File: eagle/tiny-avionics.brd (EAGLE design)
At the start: 65.8 x 25.4 mm, 60 parts, among them J1 USB-MICROB, J3 JST-PH-2-SMT-RA, U1 LP5907, U5 LTC1998, U6 ATMEGA32U4-AU, X1 8MHz

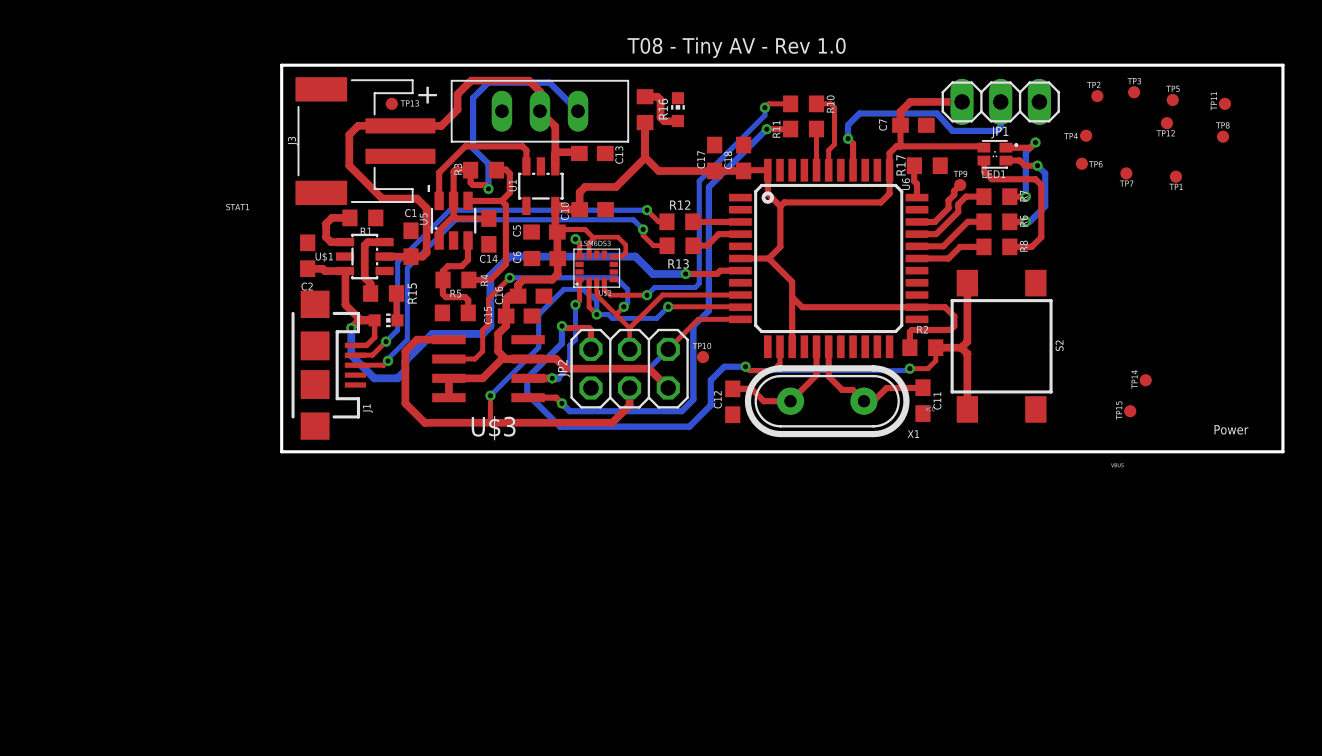
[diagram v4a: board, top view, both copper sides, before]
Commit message: Finished new board layout with no DRC errors.
It's a little smaller, but not much smaller.  Made an effort to spread out
components for easier assembly, however.  Layout is also much more
intuitive.
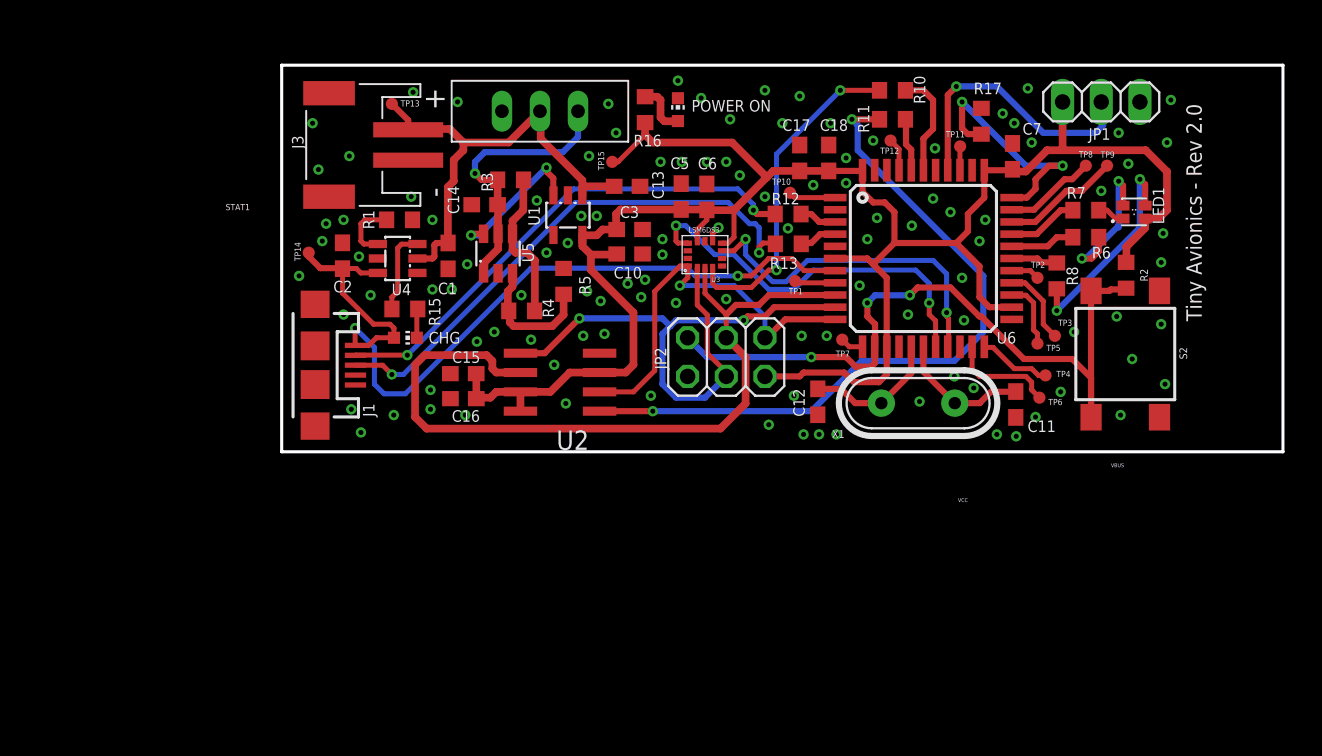
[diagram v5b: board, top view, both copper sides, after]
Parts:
- removed U$1: BQ21040, tinyav-lib:SOT23-6L
- removed U$2: LSM6DS3, tinyav-lib:LGA-14L
- removed U$3: M25PX16, tinyav-lib:SO8
- added C3: 2.2µ, rcl:C0603
- added U2: M25PX16, tinyav-lib:SO8
- added U3: LSM6DS3, tinyav-lib:LGA-14L
- added U4: BQ21040, tinyav-lib:SOT23-6L
- moved TP14 55.6 mm to (1.78, 13.1)
- moved TP15 37.8 mm to (21.7, 19.1)
- moved TP1 25.9 mm to (33.7, 11.2)
- moved TP7 21.6 mm to (36.8, 7.37)
- moved TP5 18.3 mm to (49.7, 7.11)
- moved TP12 18.2 mm to (40.0, 20.4)
- moved TP11 17.6 mm to (44.6, 20.1)
- moved TP3 16.8 mm to (50.8, 7.62)
- moved TP4 16.0 mm to (50.2, 5.02)
- moved TP6 15.6 mm to (49.8, 3.56)
- moved R2 14.2 mm to (55.5, 11.6), turned to 90 degrees
- moved TP2 12.6 mm to (49.7, 11.4)
- moved TP10 12.2 mm to (33.4, 17.0)
- moved C6 11.4 mm to (27.9, 16.7), turned to 90 degrees
- moved LED1 9.91 mm to (56.0, 15.7), turned to 90 degrees
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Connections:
- net CLK: now also U2.6, U3.13; no longer U$2.13, U$3.6
- net GND: now also C3.2, U2.4, U3.2, U3.3, U3.6, U3.7, U4.5; no longer U$1.5, U$2.2, U$2.3, U$2.6, U$2.7, U$3.4
- net MEM_EN: now also U2.1; no longer U$3.1
- net MISO: now also U2.2, U3.1; no longer U$2.1, U$3.2
- net MOSI: now also U2.5, U3.14; no longer U$2.14, U$3.5
- net N$10: now also U3.4; no longer U$2.4
- net N$11: now also U3.9; no longer U$2.9
- net N$13: now also U4.2; no longer U$1.2
- net N$4: now also U4.3; no longer U$1.3
- net N$49: now also U4.4; no longer U$1.4
- net VBUS1: now also U4.6; no longer U$1.6
- net VCC: now also C3.1, U2.3, U2.7, U2.8, U3.5, U3.8; no longer U$2.5, U$2.8, U$3.3, U$3.7, U$3.8
- net XM_EN: now also U3.12; no longer U$2.12
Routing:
- net N$10: track 1.27 -> 25.4 mm, vias 1 -> 2
- net N$11: track 0.00 -> 22.6 mm, vias 0 -> 2
- net CLK: track 31.6 -> 51.8 mm, vias 2 -> 0
- net VCC: track 114.5 -> 131.7 mm
- net N$65: track 2.18 -> 16.1 mm, vias 0 -> 2
- net MEM_EN: track 32.9 -> 46.7 mm
- net MOSI: track 49.9 -> 39.4 mm, vias 3 -> 2
- net VBUS1: track 45.6 -> 54.9 mm
- net D+: track 28.2 -> 35.4 mm
- net N$15: track 25.1 -> 18.1 mm
- net TP6: track 0.00 -> 6.96 mm
- net N$13: track 36.9 -> 30.7 mm
- net TP8: track 0.00 -> 6.07 mm
- net N$3: track 54.2 -> 48.2 mm
- net D-: track 27.3 -> 33.0 mm
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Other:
- board text added: "CHG"
- board text added: "POWER ON"
- board text added: "Tiny Avionics - Rev 2.0"
- board text removed: "Power"
- board text removed: "T08 - Tiny AV - Rev 1.0"

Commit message: Some minor changes.
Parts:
- moved R2 0.13 mm to (55.5, 11.5)
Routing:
- net GND: vias 111 -> 112
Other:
- board text removed: "STAT1"
- board text removed: "VBUS"
- board text removed: "VCC"
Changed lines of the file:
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@@
 <text x="59.436" y="22.86" size="1.016" layer="21" font="vector" rot="R270">Tiny Avionics - Rev 2.0</text>
 <text x="26.924" y="22.352" size="0.762" layer="21">POWER ON</text>
-<text x="-3.683" y="15.875" size="0.4064" layer="21">STAT1</text>
-<text x="54.483" y="-1.016" size="0.254" layer="21" font="vector">VBUS</text>
-<text x="45.085" y="-3.048" size="0.254" layer="21" font="vector" rot="R180">VCC</text>
 <text x="23.495" y="27.94" size="1.778" layer="150">Tiny AV Board Layout
 Rev: 1.0
@@
 <attribute name="NAME" x="36.987" y="1.418" size="0.508" layer="25" ratio="10" rot="R180"/>
 </element>
-<element name="R2" library="rcl" package="R0603" value="10k" x="55.481" y="11.597" smashed="yes" rot="R90">
-<attribute name="NAME" x="56.406" y="12.025" size="0.508" layer="25" ratio="10" rot="R270"/>
+<element name="R2" library="rcl" package="R0603" value="10k" x="55.481" y="11.47" smashed="yes" rot="R90">
+<attribute name="NAME" x="56.406" y="11.898" size="0.508" layer="25" ratio="10" rot="R270"/>
 </element>
 <element name="JP1" library="pinhead" package="1X03" value="" x="53.848" y="22.987" smashed="yes">
@@
 <via x="8.636" y="23.622" extent="1-16" drill="0.3302"/>
 <via x="4.064" y="9.017" extent="1-16" drill="0.3302"/>
+<via x="48.514" y="7.62" extent="1-16" drill="0.3302"/>
 <wire x1="26.683" y1="13.204" x2="27.813" y2="13.834" width="0" layer="19" extent="1-1"/>
-<wire x1="47.964" y1="8.7" x2="44.831" y2="8.636" width="0" layer="19" extent="1-1"/>
 </signal>
 <signal name="CLK">
@@
 <wire x1="56.732" y1="14.695" x2="55.499" y2="13.462" width="0.508" layer="1"/>
 <wire x1="55.499" y1="13.462" x2="55.499" y2="12.465" width="0.508" layer="1"/>
-<wire x1="55.499" y1="12.465" x2="55.481" y2="12.447" width="0.508" layer="1"/>
+<wire x1="55.499" y1="12.465" x2="55.481" y2="12.32" width="0.508" layer="1"/>
 <wire x1="56.732" y1="15.323" x2="57.614" y2="15.323" width="0.508" layer="1"/>
 <wire x1="57.614" y1="15.323" x2="58.166" y2="15.875" width="0.508" layer="1"/>
@@
 <wire x1="27.94" y1="6.223" x2="26.67" y2="7.493" width="0.4064" layer="16"/>
 <wire x1="53.178" y1="2.273" x2="53.178" y2="10.573" width="0.4064" layer="1"/>
-<wire x1="53.178" y1="10.573" x2="54.388" y2="10.573" width="0.4064" layer="1"/>
-<wire x1="54.388" y1="10.573" x2="54.483" y2="10.668" width="0.4064" layer="1"/>
-<wire x1="54.483" y1="10.668" x2="55.402" y2="10.668" width="0.4064" layer="1"/>
-<wire x1="55.402" y1="10.668" x2="55.481" y2="10.747" width="0.4064" layer="1"/>
 <wire x1="53.178" y1="2.273" x2="53.178" y2="4.861" width="0.4064" layer="1"/>
 <wire x1="53.178" y1="4.861" x2="51.943" y2="6.096" width="0.4064" layer="1"/>
@@
 <wire x1="38.989" y1="8.382" x2="38.989" y2="6.925" width="0.4064" layer="1"/>
 <wire x1="38.989" y1="6.925" x2="38.964" y2="6.9" width="0.4064" layer="1"/>
+<wire x1="53.178" y1="10.573" x2="55.481" y2="10.573" width="0.4064" layer="1"/>
+<wire x1="55.481" y1="10.573" x2="55.481" y2="10.62" width="0.4064" layer="1"/>
 </signal>
 <signal name="N$6">

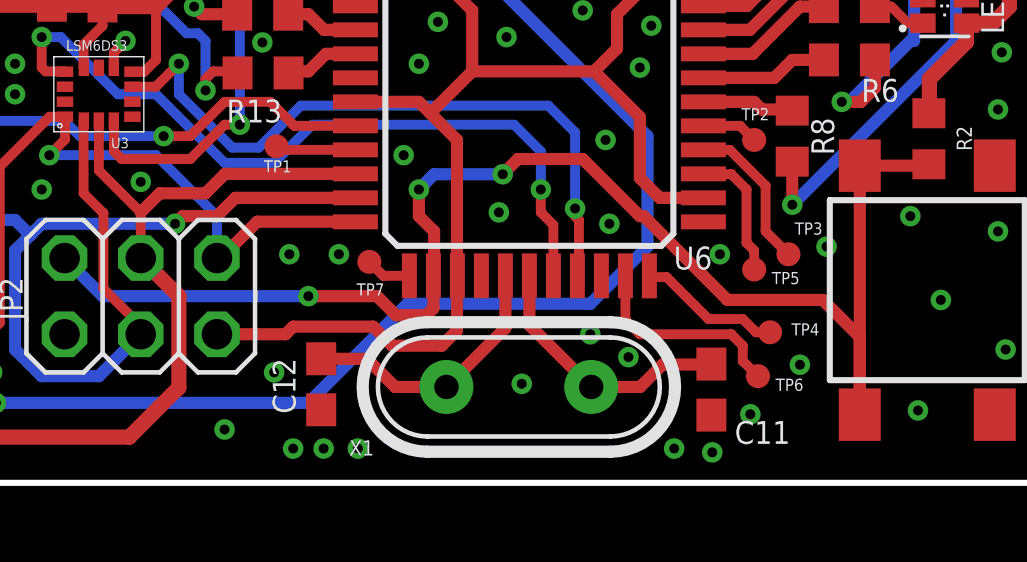
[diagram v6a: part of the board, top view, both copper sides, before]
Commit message: Added SMD crystal device and replaced on board
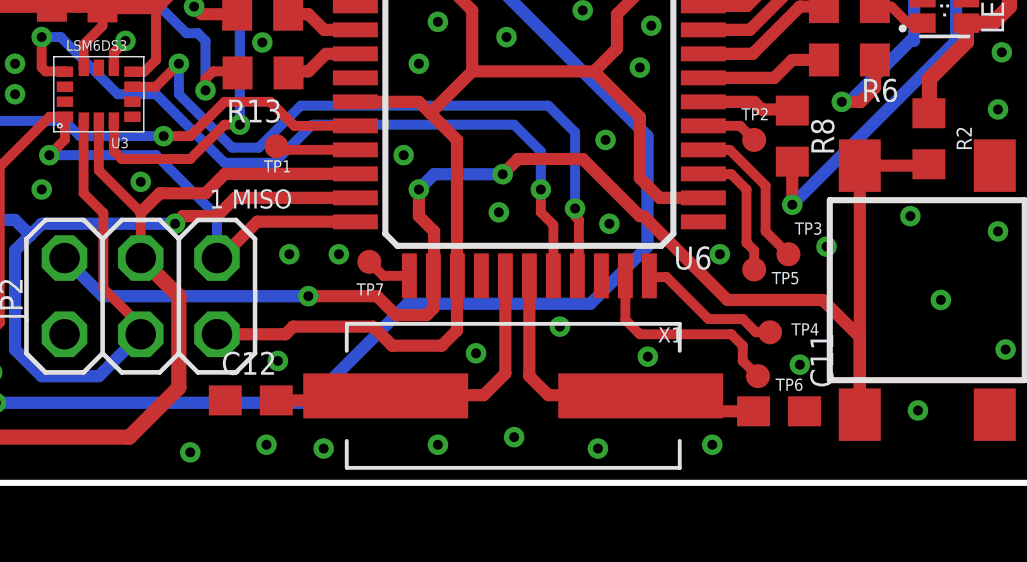
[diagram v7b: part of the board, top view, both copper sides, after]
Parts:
- X1: device IQD-Frequency-Products:HC49 -> tinyav-lib:ATS-SM
- moved C12 2.41 mm to (32.9, 2.75), turned to 180 degrees
- moved C11 2.37 mm to (50.5, 2.38), turned to 0 degrees
- moved X1 0.35 mm to (41.6, 2.90), turned to 0 degrees
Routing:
- net N$2: track 8.88 -> 11.8 mm
- net N$5: track 9.08 -> 11.3 mm
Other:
- board text added: "1 MISO"
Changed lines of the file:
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@@
 Team 08</text>
 <text x="9.652" y="7.112" size="0.762" layer="21">CHG</text>
+<text x="31.496" y="9.144" size="0.635" layer="21" font="vector">1 MISO</text>
 </plain>
 <attributes>
@@
 <attribute name="NAME" x="23.668" y="12.147" size="0.762" layer="25" rot="R180"/>
 </element>
-<element name="C11" library="rcl" package="C0603" value="22p" x="48.231" y="3.108" smashed="yes" rot="R270">
-<attribute name="NAME" x="50.86" y="2.061" size="0.762" layer="25" rot="R180"/>
-</element>
-<element name="C12" library="rcl" package="C0603" value="22p" x="35.225" y="3.286" smashed="yes" rot="R270">
-<attribute name="NAME" x="34.371" y="2.302" size="0.762" layer="25" rot="R90"/>
+<element name="C11" library="rcl" package="C0603" value="22p" x="50.486" y="2.384" smashed="yes">
+<attribute name="NAME" x="51.533" y="5.013" size="0.762" layer="25" rot="R270"/>
+</element>
+<element name="C12" library="rcl" package="C0603" value="22p" x="32.877" y="2.748" smashed="yes" rot="R180">
+<attribute name="NAME" x="31.893" y="3.602" size="0.762" layer="25"/>
 </element>
 <element name="C13" library="rcl" package="C0603" value="1µ" x="22.696" y="17.442" smashed="yes">
@@
 <attribute name="NAME" x="48.26" y="7.874" size="0.762" layer="25" rot="R180"/>
 </element>
-<element name="X1" library="IQD-Frequency-Products" package="HC49" value="8MHz" x="41.813" y="3.196" smashed="yes" rot="R180">
-<attribute name="VENDOR_PN" value="CTX900-ND" x="41.813" y="3.196" size="0.508" layer="27" rot="R180" display="off"/>
-<attribute name="VENDOR" value="DIGIKEY" x="41.813" y="3.196" size="0.508" layer="27" rot="R180" display="off"/>
-<attribute name="MPN" value="ATS080B" x="41.813" y="3.196" size="0.508" layer="27" rot="R180" display="off"/>
-<attribute name="NAME" x="36.987" y="1.418" size="0.508" layer="25" ratio="10" rot="R180"/>
+<element name="X1" library="tinyav-lib" package="ATS-SM" value="8MHz" x="41.626" y="2.9" smashed="yes">
+<attribute name="VENDOR_PN" value="CTX900-ND" x="41.626" y="2.9" size="0.508" layer="27" display="off"/>
+<attribute name="VENDOR" value="DIGIKEY" x="41.626" y="2.9" size="0.508" layer="27" display="off"/>
+<attribute name="MPN" value="ATS080B" x="41.626" y="2.9" size="0.508" layer="27" display="off"/>
+<attribute name="NAME" x="46.452" y="4.678" size="0.508" layer="25" ratio="10"/>
 </element>
 <element name="R2" library="rcl" package="R0603" value="10k" x="55.481" y="11.47" smashed="yes" rot="R90">
@@
 <via x="35.814" y="7.62" extent="1-16" drill="0.3302"/>
 <via x="34.163" y="7.62" extent="1-16" drill="0.3302"/>
-<via x="34.29" y="1.143" extent="1-16" drill="0.3302"/>
+<via x="33.401" y="1.27" extent="1-16" drill="0.3302"/>
 <via x="35.306" y="1.143" extent="1-16" drill="0.3302"/>
-<via x="36.449" y="1.143" extent="1-16" drill="0.3302"/>
-<via x="46.99" y="1.143" extent="1-16" drill="0.3302"/>
-<via x="48.26" y="1.016" extent="1-16" drill="0.3302"/>
-<via x="49.53" y="2.286" extent="1-16" drill="0.3302"/>
+<via x="39.116" y="1.27" extent="1-16" drill="0.3302"/>
+<via x="44.45" y="1.143" extent="1-16" drill="0.3302"/>
+<via x="48.26" y="1.27" extent="1-16" drill="0.3302"/>
+<via x="41.656" y="1.524" extent="1-16" drill="0.3302"/>
 <via x="55.118" y="2.413" extent="1-16" drill="0.3302"/>
 <via x="51.181" y="3.937" extent="1-16" drill="0.3302"/>
@@
 <via x="34.925" y="17.526" extent="1-16" drill="0.3302"/>
 <via x="41.402" y="14.859" extent="1-16" drill="0.3302"/>
-<via x="45.466" y="4.191" extent="1-16" drill="0.3302"/>
-<via x="44.196" y="4.953" extent="1-16" drill="0.3302"/>
-<via x="41.91" y="3.302" extent="1-16" drill="0.3302"/>
+<via x="46.112" y="4.206" extent="1-16" drill="0.3302"/>
+<via x="43.18" y="5.207" extent="1-16" drill="0.3302"/>
+<via x="40.386" y="4.318" extent="1-16" drill="0.3302"/>
 <via x="12.827" y="7.239" extent="1-16" drill="0.3302"/>
 <via x="17.907" y="5.715" extent="1-16" drill="0.3302"/>
@@
 <via x="1.143" y="11.557" extent="1-16" drill="0.3302"/>
 <via x="58.039" y="4.445" extent="1-16" drill="0.3302"/>
-<via x="33.655" y="3.683" extent="1-16" drill="0.3302"/>
+<via x="33.782" y="4.064" extent="1-16" drill="0.3302"/>
 <via x="24.257" y="3.683" extent="1-16" drill="0.3302"/>
 <via x="21.209" y="7.747" extent="1-16" drill="0.3302"/>
@@
 <via x="16.383" y="7.366" extent="1-16" drill="0.3302"/>
 <via x="19.812" y="7.62" extent="1-16" drill="0.3302"/>
-<via x="32.004" y="1.778" extent="1-16" drill="0.3302"/>
+<via x="30.861" y="1.016" extent="1-16" drill="0.3302"/>
 <via x="4.572" y="2.794" extent="1-16" drill="0.3302"/>
 <via x="33.264" y="14.679" extent="1-16" drill="0.3302"/>
@@
 <contactref element="X1" pad="1"/>
 <contactref element="C11" pad="1"/>
-<wire x1="42.164" y1="6.9" x2="42.164" y2="5.258" width="0.4064" layer="1"/>
-<wire x1="42.164" y1="5.258" x2="44.226" y2="3.196" width="0.4064" layer="1"/>
-<wire x1="44.226" y1="3.196" x2="45.857" y2="3.196" width="0.4064" layer="1"/>
-<wire x1="45.857" y1="3.196" x2="46.605" y2="3.944" width="0.4064" layer="1"/>
-<wire x1="46.605" y1="3.944" x2="48.217" y2="3.944" width="0.4064" layer="1"/>
-<wire x1="48.217" y1="3.944" x2="48.231" y2="3.958" width="0.4064" layer="1"/>
+<wire x1="42.164" y1="6.9" x2="42.164" y2="3.556" width="0.4064" layer="1"/>
+<wire x1="42.164" y1="3.556" x2="42.799" y2="2.921" width="0.4064" layer="1"/>
+<wire x1="42.799" y1="2.921" x2="45.339" y2="2.921" width="0.4064" layer="1"/>
+<wire x1="45.339" y1="2.921" x2="45.855" y2="2.921" width="0.4064" layer="1"/>
+<wire x1="45.855" y1="2.921" x2="45.876" y2="2.9" width="0.4064" layer="1"/>
+<wire x1="49.636" y1="2.384" x2="45.876" y2="2.384" width="0.4064" layer="1"/>
+<wire x1="45.876" y1="2.384" x2="45.339" y2="2.921" width="0.4064" layer="1"/>
 </signal>
 <signal name="N$5">
@@
 <contactref element="X1" pad="2"/>
 <contactref element="C12" pad="1"/>
-<wire x1="41.364" y1="6.9" x2="41.364" y2="5.16" width="0.4064" layer="1"/>
-<wire x1="41.364" y1="5.16" x2="39.4" y2="3.196" width="0.4064" layer="1"/>
-<wire x1="39.4" y1="3.196" x2="37.686" y2="3.196" width="0.4064" layer="1"/>
-<wire x1="37.686" y1="3.196" x2="36.748" y2="4.134" width="0.4064" layer="1"/>
-<wire x1="36.748" y1="4.134" x2="35.227" y2="4.134" width="0.4064" layer="1"/>
-<wire x1="35.227" y1="4.134" x2="35.225" y2="4.136" width="0.4064" layer="1"/>
+<wire x1="41.364" y1="6.9" x2="41.364" y2="3.645" width="0.4064" layer="1"/>
+<wire x1="41.364" y1="3.645" x2="40.64" y2="2.921" width="0.4064" layer="1"/>
+<wire x1="40.64" y1="2.921" x2="37.397" y2="2.921" width="0.4064" layer="1"/>
+<wire x1="37.397" y1="2.921" x2="37.376" y2="2.9" width="0.4064" layer="1"/>
+<wire x1="33.727" y1="2.748" x2="37.224" y2="2.748" width="0.4064" layer="1"/>
+<wire x1="37.224" y1="2.748" x2="37.376" y2="2.9" width="0.4064" layer="1"/>
 </signal>
 <signal name="N$13">
